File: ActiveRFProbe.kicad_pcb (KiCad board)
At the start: 2 copper layers, 100 x 35 mm, 70 parts, among them J1 Conn_01x01, J10 Conn_01x01, J11 Conn_01x01, J12 Conn_01x01, J13 Conn_01x01, J14 Conn_01x01, J15 Conn_01x01, J16 Conn_01x01, J17 Conn_01x01, J18 Conn_01x01, J19 Conn_01x01, J2 Conn_01x01, J20 Conn_01x01, J21 Conn_01x01, J22 Conn_01x01, J23 Conn_01x01, J24 Conn_01x01, J25 Conn_Coaxial, J3 Conn_01x01, J4 Conn_01x01, J5 Conn_01x01, J6 Conn_01x01, J7 Conn_01x01, J8 Conn_01x01, J9 Conn_01x01, Q1 S9018, Q2 S9018, Q3 S9018, Q4 MMBT3904, Q6 MMBT3904, Q7 MMBT3906, SW2 SW_DPDT_x2

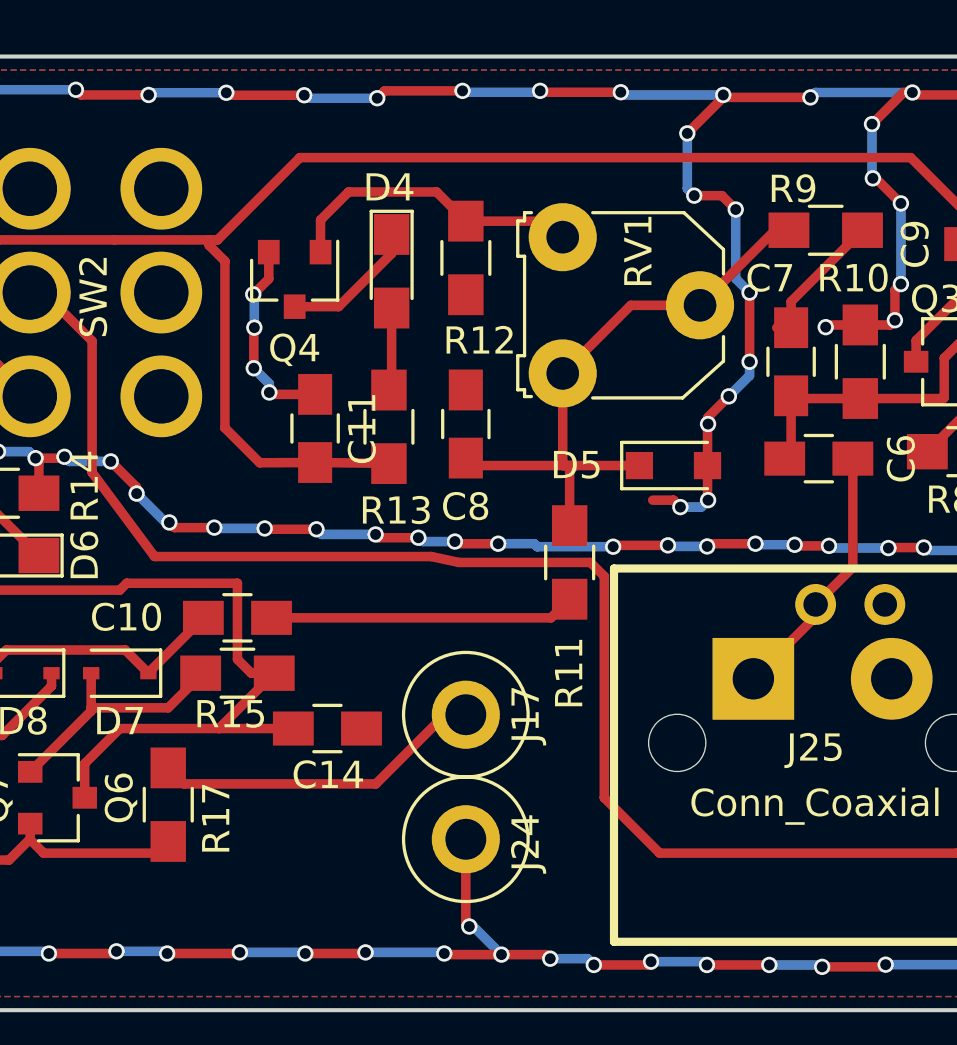
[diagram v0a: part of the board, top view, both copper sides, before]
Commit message: Fixed envelope detector
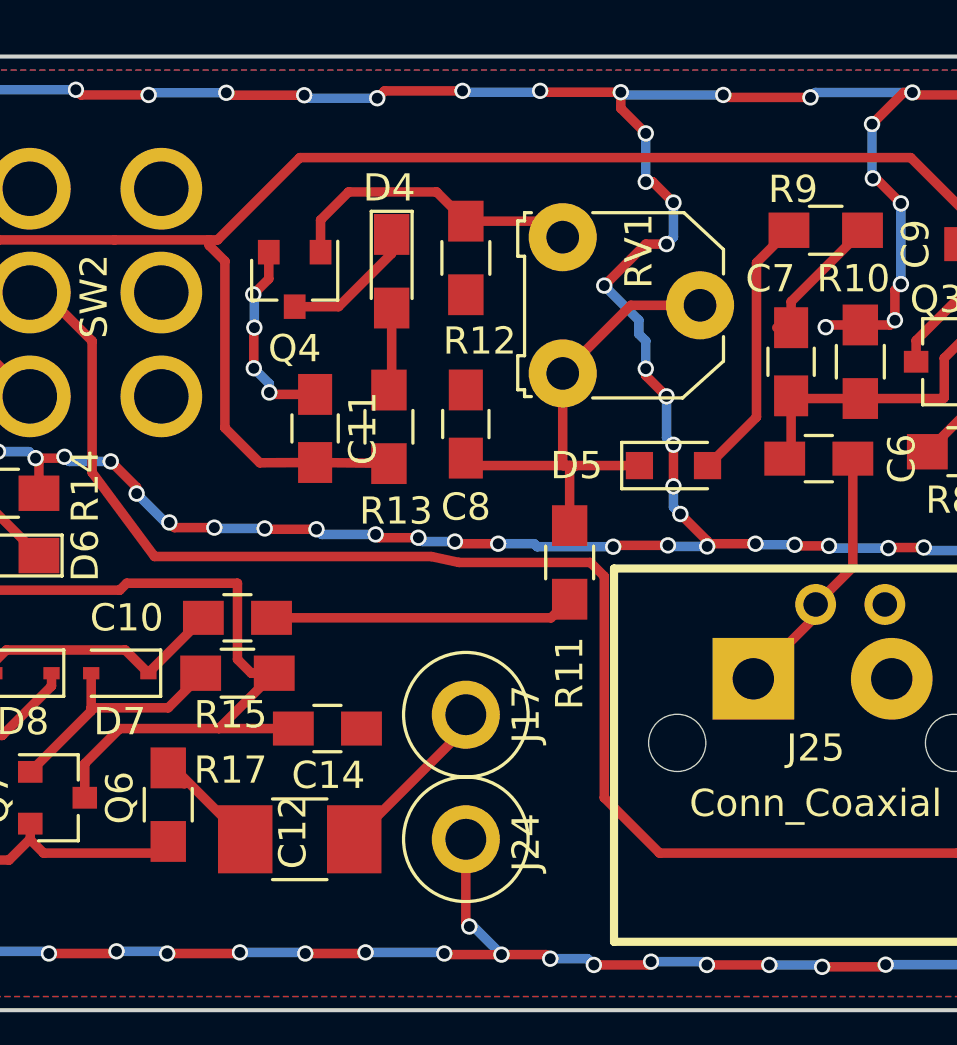
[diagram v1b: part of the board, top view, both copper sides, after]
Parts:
- added C12: 22 uF, Capacitors_SMD:C_1210_HandSoldering, F.Cu at (62.0, 109.7)
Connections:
- D5 pad 2: GND -> Net-(D5-Pad2)
- J17 pad 1: Net-(J17-Pad1) -> Net-(C12-Pad2)
- R17 pad 1: Net-(J17-Pad1) -> Net-(C12-Pad1)
- R9 pad 1: Net-(C8-Pad2) -> Net-(D5-Pad2)
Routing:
- net Net-(J17-Pad1): track 12.2 -> 0.00 mm
- net Net-(D5-Pad2): track 0.00 -> 10.4 mm
- net Net-(C12-Pad2): track 0.00 -> 7.03 mm
- net Net-(C12-Pad1): track 0.00 -> 4.74 mm
- net Net-(C8-Pad2): track 23.1 -> 18.7 mm
- net GND: track 448.2 -> 449.1 mm, vias 201 -> 202

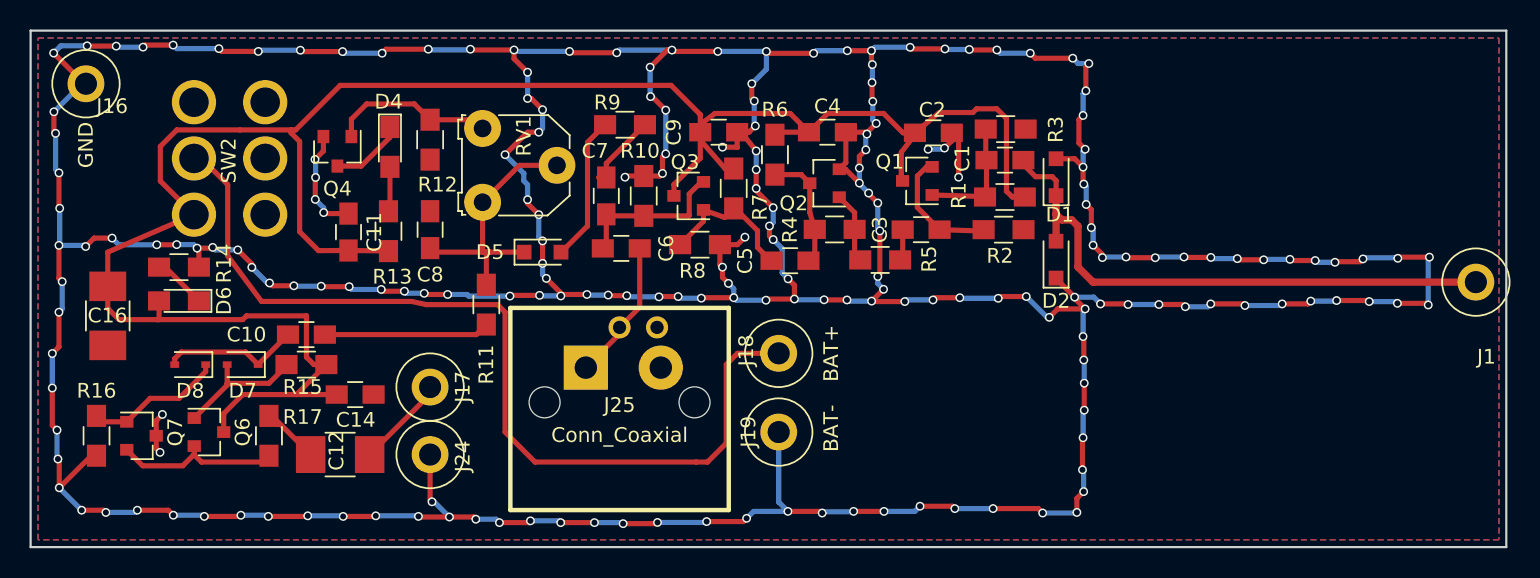
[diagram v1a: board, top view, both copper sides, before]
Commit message: Made the board smaller
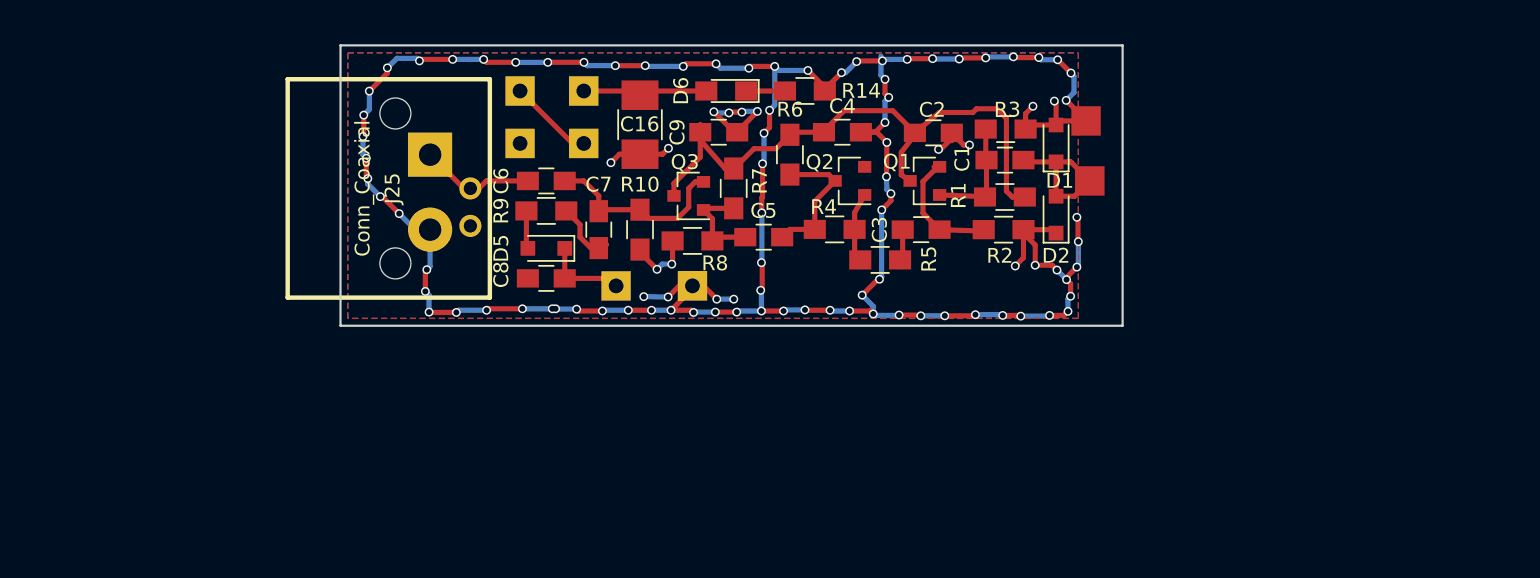
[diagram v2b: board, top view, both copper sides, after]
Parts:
- removed C10, C11: 100 nF, Capacitors_SMD:C_0805_HandSoldering
- removed C12: 22 uF, Capacitors_SMD:C_1210_HandSoldering
- removed C14: 1 uF, Capacitors_SMD:C_0805_HandSoldering
- removed D4: LED, LEDs:LED_0805_HandSoldering
- removed D7, D8: 1N4148WS, Diodes_SMD:D_SOD-323
- removed J10, J11, J12, J13, J14, J15, J4, J5, J6, J7, J8, J9: Conn_01x01, ActiveRFProbe:BigSlot
- removed Q4, Q6: MMBT3904, TO_SOT_Packages_SMD:SOT-23
- removed Q7: MMBT3906, TO_SOT_Packages_SMD:SOT-23
- removed R11, R13: 1k, Resistors_SMD:R_0805_HandSoldering
- removed R12, R15, R16: 10k, Resistors_SMD:R_0805_HandSoldering
- removed R17: 100R, Resistors_SMD:R_0805_HandSoldering
- removed RV1: 100k, Potentiometers:Potentiometer_Triwood_RM-065
- removed SW2: SW_DPDT_x2, ActiveRFProbe:DPDTsmallswitch
- J1, J16, J17, J18, J19, J24: footprint Connectors:1pin -> ActiveRFProbe:PadHole
- J2, J3: footprint ActiveRFProbe:BigSlot -> ActiveRFProbe:PadHole
- R9: value 1k -> 10k
- moved J16 67.8 mm to (112.5, 87.1)
- moved J2 60.6 mm to (78.5, 85.1)
- moved J3 58.9 mm to (74.2, 85.1)
- moved R14 44.1 mm to (93.5, 85.1)
- moved D6 39.7 mm to (88.1, 85.1)
- moved C16 38.3 mm to (82.3, 87.4)
- moved J25 31.3 mm to (58.4, 91.7), turned to 270 degrees
- moved J1 27.0 mm to (112.8, 91.2)
- moved J19 26.3 mm to (74.2, 88.6)
- moved J24 21.1 mm to (85.9, 98.3)
- moved J18 19.4 mm to (78.5, 88.6)
- moved J17 14.3 mm to (80.7, 98.3)
- moved J21 11.4 mm to (102.1, 98.7)
- moved J20 11.4 mm to (108.5, 98.6)
- moved C8 8.54 mm to (75.9, 97.8), turned to 0 degrees
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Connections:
- C16 pad 2: +9V -> Net-(C16-Pad2)
- D6 pad 2: +9V -> Net-(C16-Pad2)
- J17 pad 1: Net-(C12-Pad2) -> Net-(C8-Pad2)
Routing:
- net GND: track 449.1 -> 211.1 mm, vias 202 -> 102
- net +9V: track 147.0 -> 41.4 mm
- net Net-(J18-Pad1): track 62.1 -> 5.79 mm
- net Net-(C1-Pad2): track 39.1 -> 10.1 mm
- net Net-(C8-Pad2): track 18.7 -> 5.72 mm
- net Net-(Q6-Pad2): track 11.4 -> 0.00 mm
- net Net-(C10-Pad2): track 11.2 -> 0.00 mm
- net Net-(Q4-Pad1): track 11.2 -> 0.00 mm
- net Net-(C10-Pad1): track 9.47 -> 0.00 mm
- net Net-(D8-Pad1): track 9.45 -> 0.00 mm
- net Net-(D7-Pad2): track 9.14 -> 0.00 mm
- net Net-(C16-Pad2): track 0.00 -> 8.54 mm
- net Net-(D5-Pad2): track 10.4 -> 2.58 mm
- net Net-(C12-Pad2): track 7.03 -> 0.00 mm
- net Net-(D4-Pad1): track 5.07 -> 0.00 mm
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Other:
- board size 100 x 35 mm -> 53 x 19 mm
- board text added: "+"
- board text added: "ENVELOPE"
- board text added: "SW"

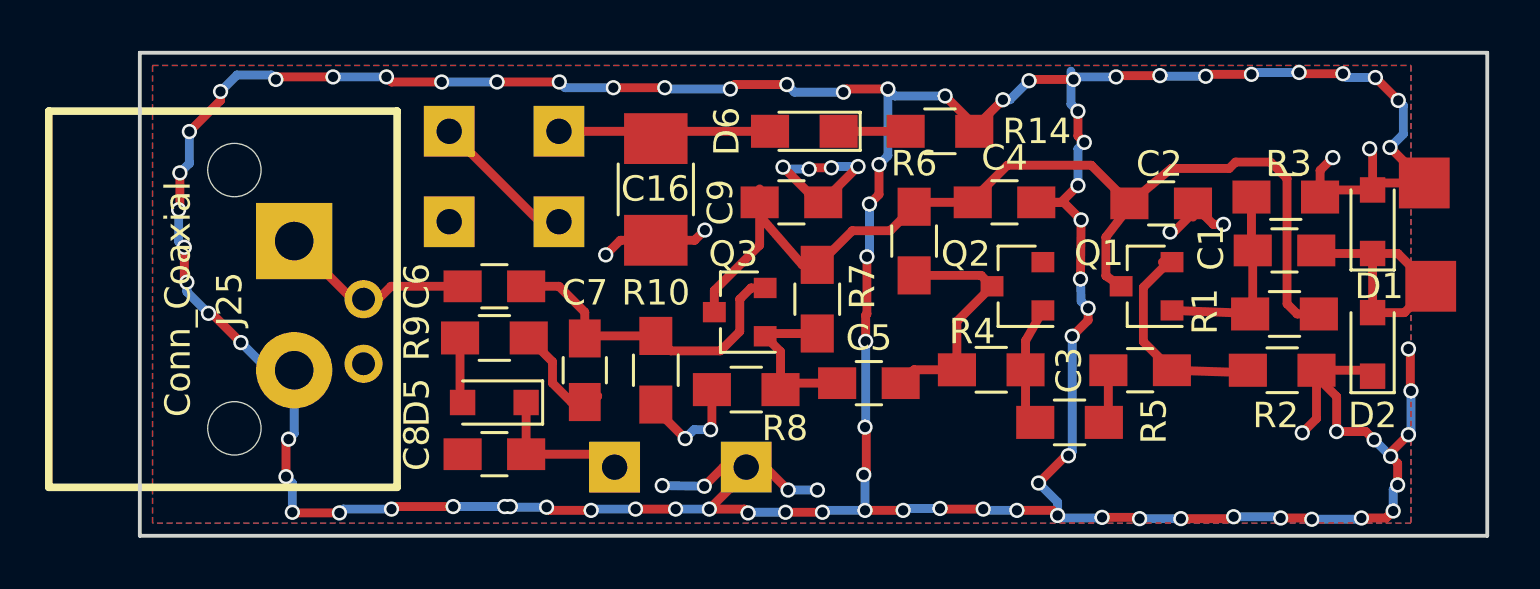
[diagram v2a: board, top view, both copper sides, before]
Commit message: Changed transistor to 2SC4083
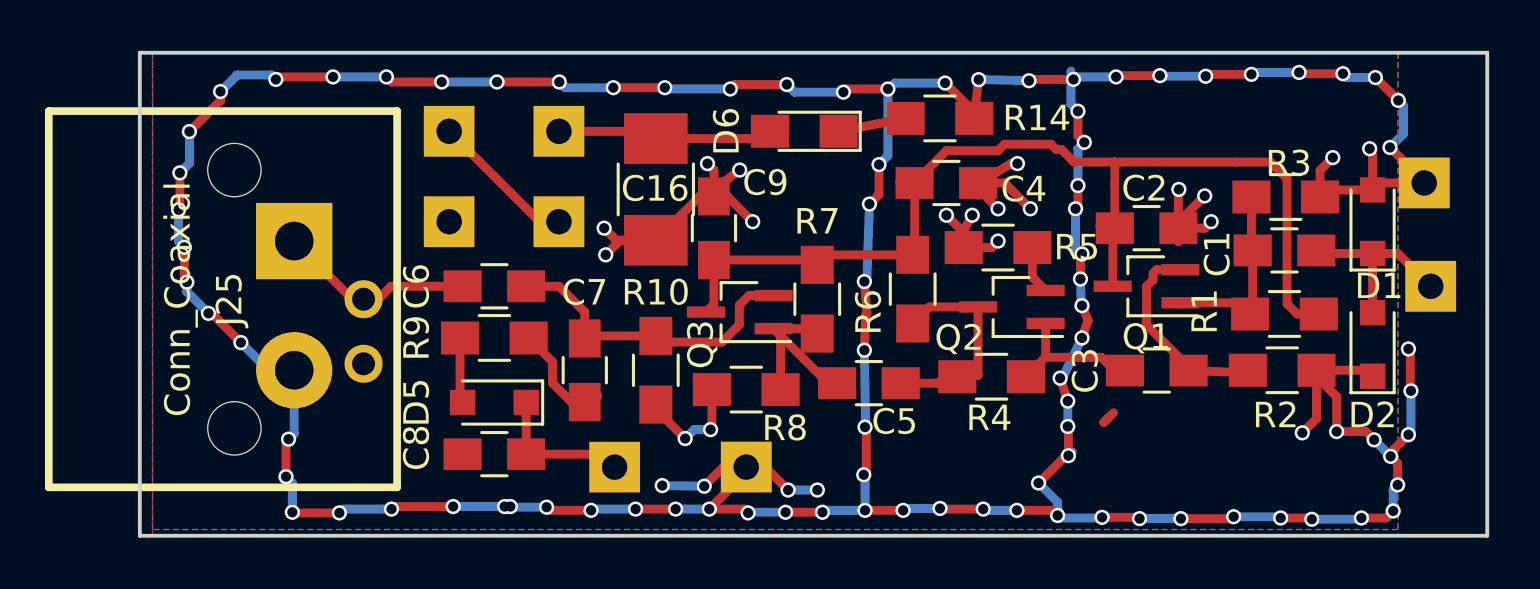
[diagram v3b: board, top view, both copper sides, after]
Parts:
- Q1, Q2, Q3: value S9018 -> BFU520W; footprint TO_SOT_Packages_SMD:SOT-23 -> TO_SOT_Packages_SMD:SOT-323_SC-70_Handsoldering
- moved R5 7.43 mm to (95.8, 89.7)
- moved C9 3.21 mm to (84.6, 88.9), turned to 270 degrees
- moved C4 2.41 mm to (93.7, 87.1)
- moved R6 1.89 mm to (92.4, 91.3)
- moved C2 1.13 mm to (101.6, 88.9)
- moved Q2 0.84 mm to (96.3, 92.0)
- moved C3 0.65 mm to (102.0, 94.5)
- moved R14 0.51 mm to (93.5, 84.6)
- moved R4 0.27 mm to (95.5, 94.7)
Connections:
- Q2 pad 1: Net-(Q2-Pad1) -> Net-(C3-Pad1)
- Q2 pad 2: GND -> Net-(Q2-Pad2)
- R4 pad 2: Net-(Q2-Pad1) -> Net-(C3-Pad1)
- R5 pad 1: Net-(Q2-Pad1) -> GND
- R5 pad 2: Net-(C3-Pad1) -> Net-(Q2-Pad2)
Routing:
- net GND: track 211.1 -> 223.8 mm, vias 102 -> 112
- net Net-(Q2-Pad1): track 5.05 -> 0.00 mm
- net Net-(C3-Pad1): track 2.66 -> 6.81 mm
- net Net-(C1-Pad2): track 10.1 -> 7.41 mm
- net +9V: track 41.4 -> 43.3 mm
- net Net-(Q2-Pad2): track 0.00 -> 1.90 mm
- net Net-(C5-Pad1): track 7.03 -> 8.16 mm
- net (no net): track 0.00 -> 0.79 mm
- net Net-(C6-Pad2): track 13.8 -> 13.2 mm

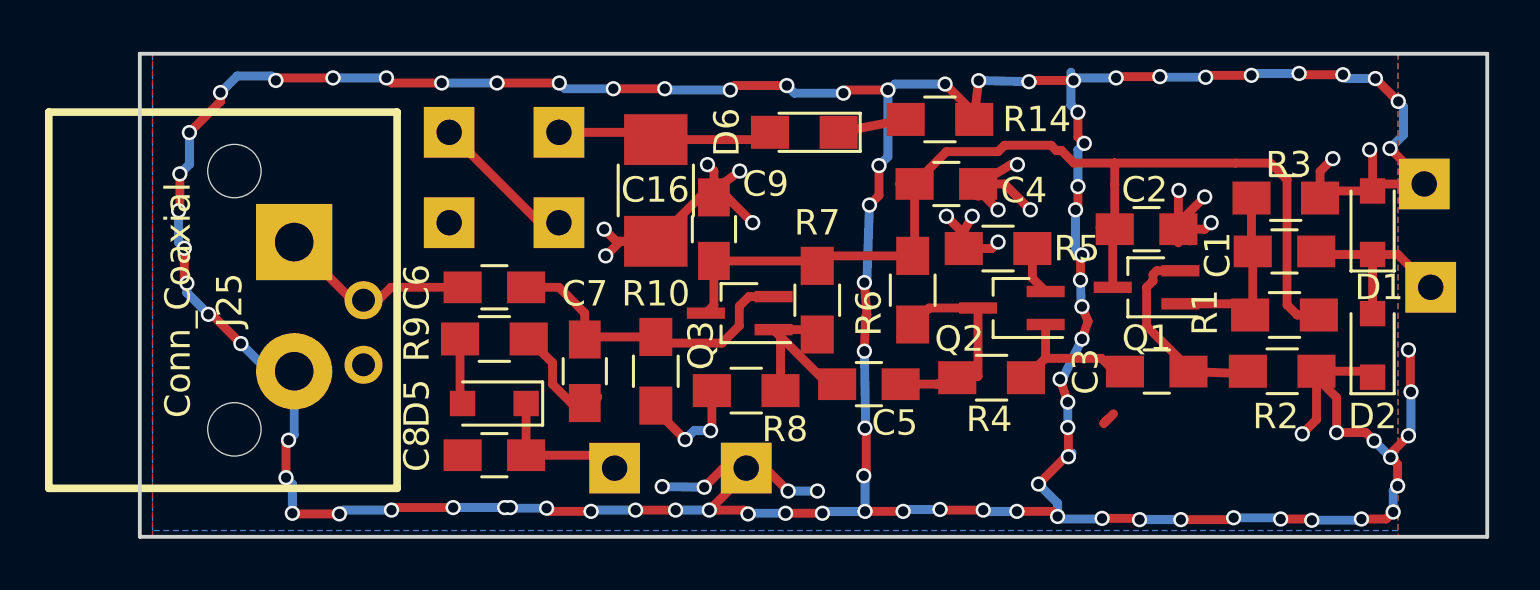
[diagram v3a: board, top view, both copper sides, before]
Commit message: Version with SOT-232 2SC4083
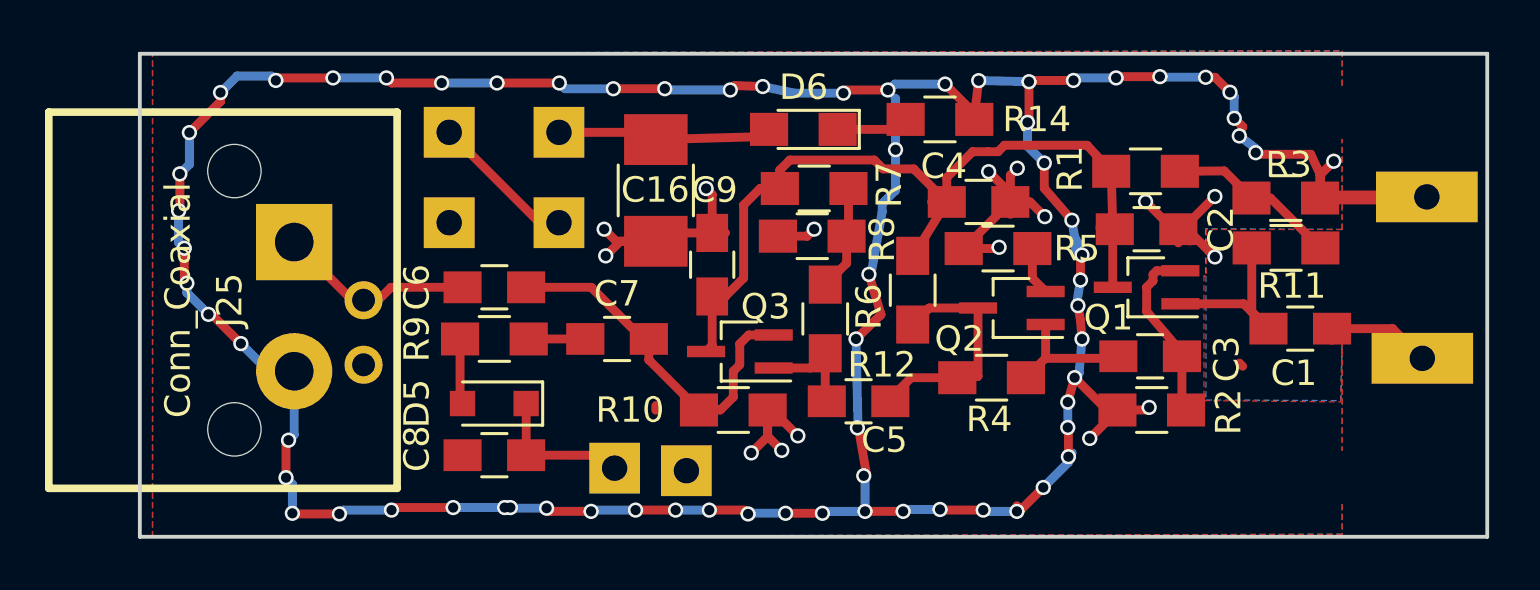
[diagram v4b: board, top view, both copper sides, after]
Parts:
- removed D1, D2: 1N4148WS, Diodes_SMD:D_SOD-323_HandSoldering
- added R11: 10k, Resistors_SMD:R_0805_HandSoldering, F.Cu at (107.1, 89.6)
- added R12: 1k, Resistors_SMD:R_0805_HandSoldering, F.Cu at (89.0, 92.4)
- Q1, Q2, Q3: value BFU520W -> 2SC4083
- moved R1 7.86 mm to (101.6, 86.6), turned to 0 degrees
- moved R8 6.61 mm to (88.5, 89.2)
- moved R2 5.35 mm to (101.8, 96.0), turned to 180 degrees
- moved R7 4.40 mm to (88.5, 87.3), turned to 0 degrees
- moved R10 3.41 mm to (85.3, 96.0), turned to 0 degrees
- moved C1 3.10 mm to (107.6, 92.8)
- moved J1 2.81 mm to (112.4, 94.0)
- moved J24 2.35 mm to (83.5, 98.4)
- moved C7 1.80 mm to (80.8, 93.2), turned to 0 degrees
- moved Q3 1.51 mm to (85.6, 93.7)
- moved C4 1.45 mm to (95.0, 87.8)
- moved C9 1.40 mm to (84.5, 90.3)
- moved C5 0.79 mm to (90.3, 95.7)
- moved C3 0.65 mm to (101.7, 93.9)
- moved J16 0.52 mm to (112.6, 87.6)
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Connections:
- R1 pad 2: Net-(C1-Pad1) -> Net-(R1-Pad2)
- R3 pad 1: Net-(C1-Pad1) -> Net-(R1-Pad2)
- R7 pad 2: Net-(C5-Pad1) -> Net-(R12-Pad2)
- R8 pad 1: Net-(C5-Pad1) -> Net-(R12-Pad2)
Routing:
- net GND: track 223.8 -> 188.1 mm, vias 112 -> 86
- net +9V: track 43.3 -> 34.3 mm
- net Net-(R1-Pad2): track 0.00 -> 6.78 mm
- net Net-(R12-Pad2): track 0.00 -> 4.16 mm
- net Net-(C5-Pad1): track 8.16 -> 4.54 mm
- net Net-(C1-Pad2): track 7.41 -> 4.50 mm
- net Net-(C7-Pad1): track 5.40 -> 2.86 mm
- net Net-(C6-Pad2): track 13.2 -> 14.5 mm
- net Net-(C5-Pad2): track 9.55 -> 10.4 mm
- net Net-(C3-Pad2): track 8.67 -> 7.99 mm
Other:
- board text added: "RF"
